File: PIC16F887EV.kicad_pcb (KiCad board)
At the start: 2 copper layers, 100 x 100 mm, 99 parts, among them P1 USB_C_Plug_USB2.0, Q1 2N3904, Q2 2N3904, Q3 2N3904, Q5 2N3904, SW1 SW_Push, SW10 SW_Push, SW11 SW_Push, SW12 SW_Push, SW13 SW_Push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

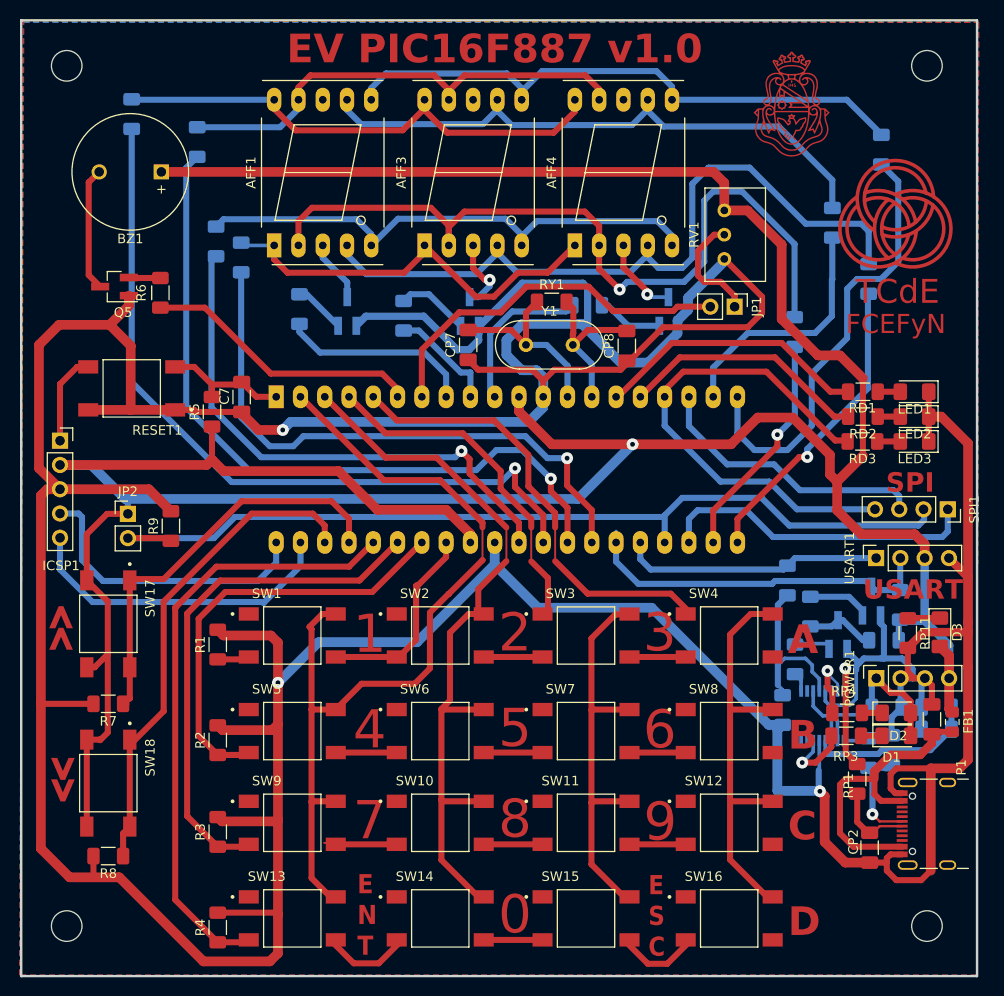
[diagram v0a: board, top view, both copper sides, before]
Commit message: Update v1.1
-Correccion USB C (pads, conexion shield, pines de datos, etc)
-Correccion footprints transistores, reruteo
-Se acomodaron los textos en silkscreen
-Zonas sin alivios termicos
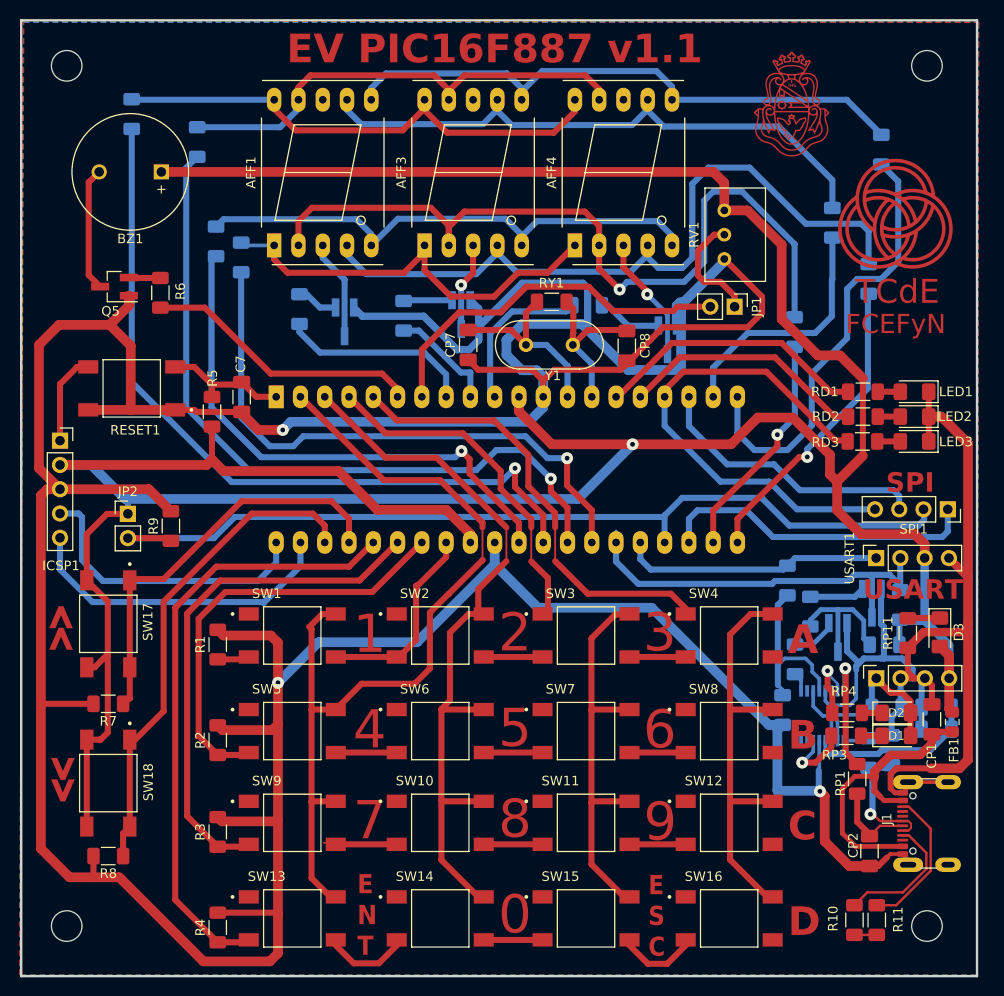
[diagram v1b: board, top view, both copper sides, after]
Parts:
- removed P1: USB_C_Plug_USB2.0, Connector_USB:USB_C_Receptacle_GCT_USB4105-xx-A_16P_TopMnt_Horizontal
- added J1: USB_C_Receptacle_USB2.0_14P, Connector_USB:USB_C_Receptacle_GCT_USB4105-xx-A_16P_TopMnt_Horizontal, F.Cu at (111.1, 99.3)
- added R10: 5.1k, Resistor_SMD:R_1206_3216Metric_Pad1.30x1.75mm_HandSolder, F.Cu at (102.4, 109.4)
- added R11: 5.1k, Resistor_SMD:R_1206_3216Metric_Pad1.30x1.75mm_HandSolder, F.Cu at (104.7, 109.4)
- Q1, Q2, Q3, Q5, QP1, QP2: footprint Package_TO_SOT_SMD:SOT-23_Handsoldering -> Huellas:SOT-23_Handsoldering-mod
- moved Q3 2.97 mm to (82.9, 48.7), turned to -90 degrees
- moved Q1 1.12 mm to (49.1, 46.8), turned to -90 degrees
- moved Q2 0.94 mm to (61.3, 46.0), turned to -90 degrees
- moved RP8 0.47 mm to (105.6, 80.6)
- moved CP2 0.36 mm to (104.0, 102.2)
- moved QP1 0.31 mm to (100.7, 79.8), turned to -90 degrees
- moved QP2 0.23 mm to (104.2, 76.2), turned to -90 degrees
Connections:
- AFF1 pad 8: Net-(Q1-C) -> unconnected-(AFF1-C.K.-Pad8)
- AFF3 pad 8: Net-(Q2-C) -> unconnected-(AFF3-C.K.-Pad8)
- AFF4 pad 8: Net-(Q3-C) -> unconnected-(AFF4-C.K.-Pad8)
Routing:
- net Net-(J1-CC2): track 0.00 -> 15.4 mm
- net Net-(J1-CC1): track 0.00 -> 14.1 mm
- net GND: track 586.5 -> 593.7 mm
- net Net-(QP1-C): track 7.29 -> 14.4 mm
- net Net-(Q3-C): track 8.49 -> 13.7 mm
- net RXpic: track 38.4 -> 43.0 mm
- net Net-(Q1-C): track 6.47 -> 10.4 mm
- net Net-(CP3-Pad1): track 11.0 -> 13.7 mm
- net Net-(Q2-B): track 7.61 -> 5.10 mm
- net e: track 43.1 -> 44.6 mm
- net Net-(Q2-C): track 7.85 -> 9.25 mm
- net Net-(QP1-B): track 3.70 -> 4.79 mm
- net Net-(Q1-B): track 5.42 -> 4.35 mm
- net Net-(CP1-Pad2): track 32.0 -> 31.3 mm
- net Net-(QP2-B): track 6.58 -> 5.83 mm
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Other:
- board text added: "EV PIC16F887 v1.1"
- board text removed: "EV PIC16F887 v1.0"

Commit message: Correccion v1.1
falto una pista
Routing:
- net Net-(CP2-Pad1): track 8.90 -> 14.1 mm
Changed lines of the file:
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@@
 		(fp_arc
 			(start -2.1747 0.3223)
-			(mid -1.600349 -4.921577)
+			(mid -1.600348 -4.921578)
 			(end 3.1903 -2.713)
 			(stroke
@@
 		(fp_arc
 			(start -2.1747 0.3223)
-			(mid -1.600349 -4.921577)
+			(mid -1.600348 -4.921578)
 			(end 3.1903 -2.713)
 			(stroke
@@
 	)
 	(segment
+		(start 102.7 97.3328)
+		(end 102.7 96.15)
+		(width 0.635)
+		(layer "F.Cu")
+		(net 77)
+	)
+	(segment
 		(start 103.9876 100.3876)
 		(end 102.7 99.1)
@@
 	)
 	(segment
+		(start 102.7 99.1)
+		(end 102.7 97.3328)
+		(width 0.635)
+		(layer "F.Cu")
+		(net 77)
+	)
+	(segment
 		(start 105.0868 99.5132)
 		(end 107.4556 99.5132)
@@
 	)
 	(segment
-		(start 102.7 99.1)
-		(end 102.7 96.15)
-		(width 0.635)
+		(start 103.9876 100.5963)
+		(end 104.0037 100.5963)
+		(width 0.254)
 		(layer "F.Cu")
 		(net 77)
 	)
 	(segment
-		(start 103.9876 100.5963)
-		(end 104.0037 100.5963)
+		(start 107.4556 98.5132)
+		(end 105.648732 98.5132)
 		(width 0.254)
 		(layer "F.Cu")
@@
 		(width 0.254)
 		(layer "F.Cu")
+		(net 77)
+	)
+	(segment
+		(start 104.468332 97.3328)
+		(end 102.7 97.3328)
+		(width 0.254)
+		(layer "F.Cu")
+		(net 77)
+	)
+	(segment
+		(start 105.648732 98.5132)
+		(end 104.468332 97.3328)
+		(width 0.254)
+		(layer "F.Cu")

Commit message: Cambio de nombre v2.0
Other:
- board text added: "EV PIC16F887 v2.0"
- board text removed: "EV PIC16F887 v1.1"
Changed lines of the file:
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@@
 		(fp_arc
 			(start -2.1747 0.3223)
-			(mid -1.600348 -4.921578)
+			(mid -1.600349 -4.921577)
 			(end 3.1903 -2.713)
 			(stroke
@@
 		(fp_arc
 			(start -2.1747 0.3223)
-			(mid -1.600348 -4.921578)
+			(mid -1.600349 -4.921577)
 			(end 3.1903 -2.713)
 			(stroke
@@
 		)
 	)
-	(gr_text "EV PIC16F887 v1.1"
+	(gr_text "EV PIC16F887 v2.0"
 		(at 43 20 0)
 		(layer "F.Cu")
@@
 		)
 	)
-	(gr_text "EV PIC16F887 v1.1"
+	(gr_text "EV PIC16F887 v2.0"
 		(at 43 20 0)
 		(layer "F.Mask")

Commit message: Revert "Cambio de nombre v2.0"
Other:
- board text added: "EV PIC16F887 v1.1"
- board text removed: "EV PIC16F887 v2.0"
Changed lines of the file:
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@@
 		(fp_arc
 			(start -2.1747 0.3223)
-			(mid -1.600349 -4.921577)
+			(mid -1.600348 -4.921578)
 			(end 3.1903 -2.713)
 			(stroke
@@
 		(fp_arc
 			(start -2.1747 0.3223)
-			(mid -1.600349 -4.921577)
+			(mid -1.600348 -4.921578)
 			(end 3.1903 -2.713)
 			(stroke
@@
 		)
 	)
-	(gr_text "EV PIC16F887 v2.0"
+	(gr_text "EV PIC16F887 v1.1"
 		(at 43 20 0)
 		(layer "F.Cu")
@@
 		)
 	)
-	(gr_text "EV PIC16F887 v2.0"
+	(gr_text "EV PIC16F887 v1.1"
 		(at 43 20 0)
 		(layer "F.Mask")
